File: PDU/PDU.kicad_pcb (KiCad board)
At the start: 2 copper layers, 111 x 127 mm, 82 parts, among them J10 Conn_01x02_Socket, J11 Screw_Terminal_01x02, J12 Conn_01x05_Pin, J2 USB_B_Micro, J3 Screw_Terminal_01x02, J4 Conn_01x03_Socket, J5 Conn_01x02_Socket, J6 Conn_01x02_Socket, J7 Conn_01x02_Socket, J8 Conn_01x02_Socket, J9 Conn_01x02_Socket, Q1 PMOS, Q2 NMOS, Q3 PMOS, U1 TPS564257DRLR, U2 MCP6002-I/P, U5 LM73100RPWR, U6 BQ25172DSGR, U8 MAX20801TPBA+, U9 TPS564257DRLR

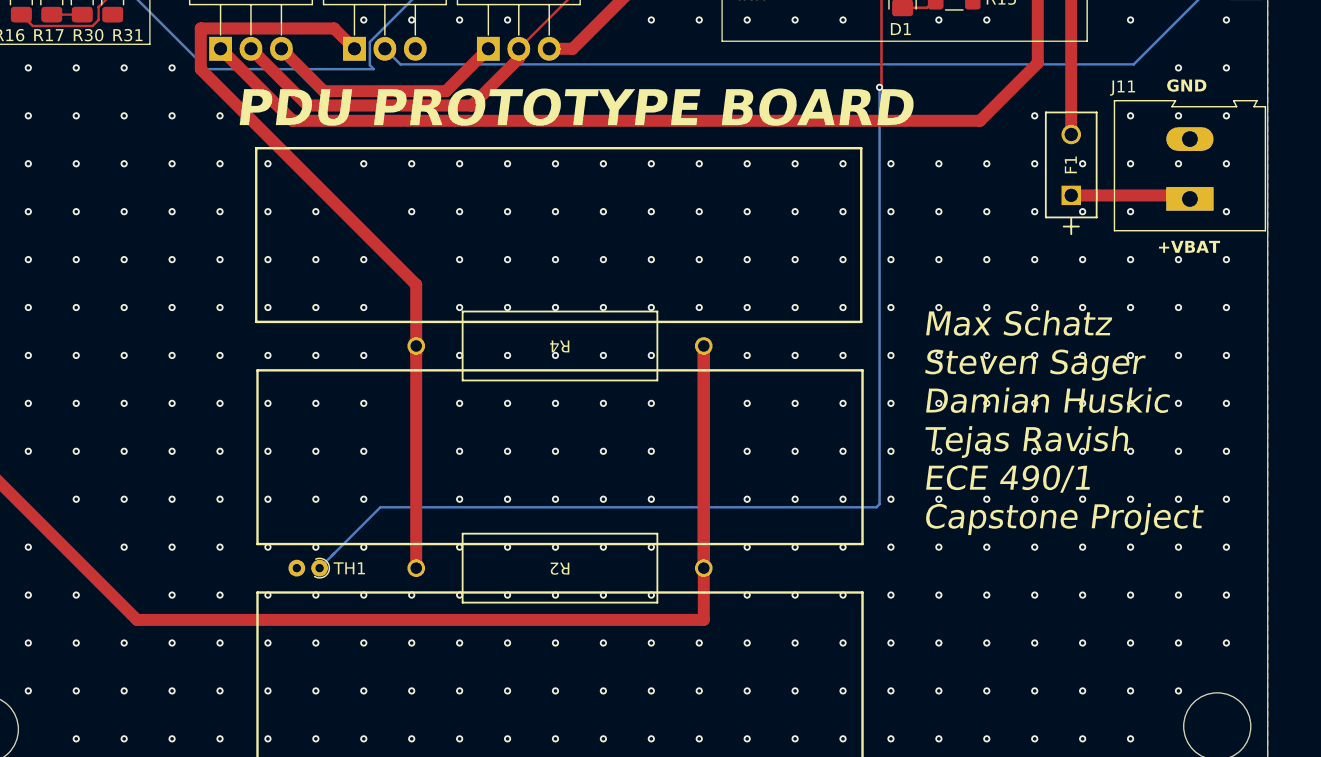
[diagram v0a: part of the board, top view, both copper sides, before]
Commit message: Made revision on PDU board before ECLASS submission
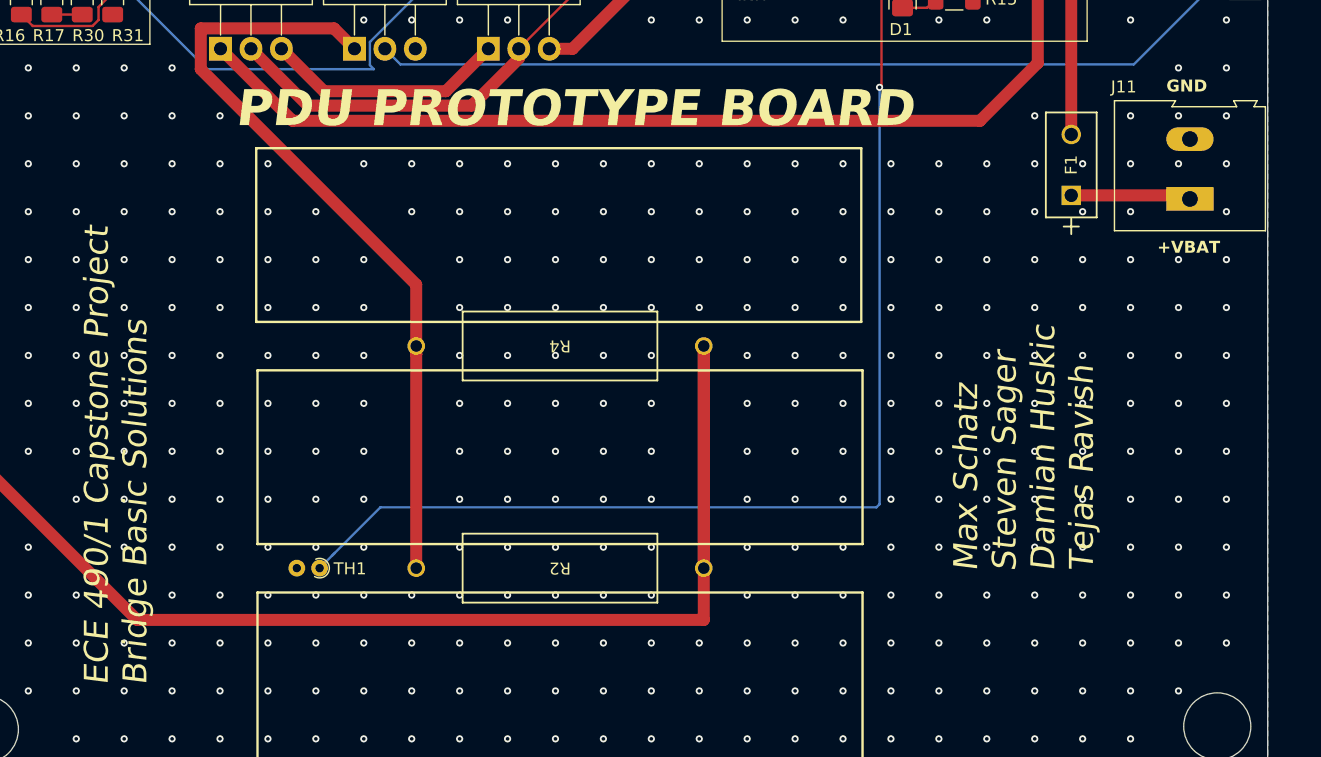
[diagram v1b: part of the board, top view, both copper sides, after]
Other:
- board text added: "ECE 490/1 Capstone Project Bridge Basic Solutions"
- board text added: "Max Schatz Steven Sager Damian Huskic Tejas Ravish"
- board text removed: "Max Schatz Steven Sager Damian Huskic Tejas Ravish ECE 490/1 Capstone Project"
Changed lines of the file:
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@@
+		)
+	)
+	(gr_text "ECE 490/1 Capstone Project\nBridge Basic Solutions"
+		(at 114.5 148.5 90)
+		(layer "F.SilkS")
+		(effects
+			(font
+				(size 2 2)
+				(thickness 0.2)
+				(italic yes)
+			)
+			(justify left bottom)
 		)
 	)
@@
 		)
 	)
-	(gr_text "Max Schatz\nSteven Sager\nDamian Huskic\nTejas Ravish\nECE 490/1\nCapstone Project"
-		(at 179.07 135.636 0)
+	(gr_text "Max Schatz\nSteven Sager\nDamian Huskic\nTejas Ravish"
+		(at 193.5 139 90)
 		(layer "F.SilkS")
 		(effects

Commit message: Last revision
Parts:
- removed C12: 1u, Capacitor_SMD:C_1206_3216Metric_Pad1.33x1.80mm_HandSolder
- removed C13: 0.22u, Capacitor_SMD:C_1206_3216Metric_Pad1.33x1.80mm_HandSolder
- removed C14, C15, C16, C17, C18: 10u, Capacitor_SMD:C_1206_3216Metric_Pad1.33x1.80mm_HandSolder
- removed J10, J7, J8, J9: Conn_01x02_Socket, Connector_PinHeader_2.54mm:PinHeader_1x02_P2.54mm_Vertical
- removed J11: Screw_Terminal_01x02, TerminalBlock:TerminalBlock_Altech_AK300-2_P5.00mm
- removed J12: Conn_01x05_Pin, Connector_PinHeader_2.54mm:PinHeader_1x05_P2.54mm_Vertical
- removed J4: Conn_01x03_Socket, Connector_PinHeader_2.54mm:PinHeader_1x03_P2.54mm_Vertical
- removed L2: 0.68uH, Capstone:IND_RR68M8A_VIS
- removed Q1: PMOS, Package_TO_SOT_THT:TO-220-3_Horizontal_TabDown
- removed Q2: NMOS, Package_TO_SOT_THT:TO-220-3_Horizontal_TabDown
- removed R2, R4: 15, Capstone:res2_1-1625892-1_TEC
- removed TH1: 10k, Resistor_THT:R_Axial_DIN0204_L3.6mm_D1.6mm_P1.90mm_Vertical
- removed U8: MAX20801TPBA+, Capstone:21-100119_MXM
- added C28: 22u, Capacitor_SMD:C_1206_3216Metric_Pad1.33x1.80mm_HandSolder, B.Cu at (145.5, 111.7)
- added C29: 100n, Capacitor_SMD:C_1206_3216Metric_Pad1.33x1.80mm_HandSolder, B.Cu at (145.5, 109.1)
- added C30: 4.7u, Capacitor_SMD:C_1206_3216Metric_Pad1.33x1.80mm_HandSolder, B.Cu at (124.2, 114.1)
- added C31: 100n, Capacitor_SMD:C_1206_3216Metric_Pad1.33x1.80mm_HandSolder, B.Cu at (124.2, 111.6)
- added C32: 100n, Capacitor_SMD:C_1206_3216Metric_Pad1.33x1.80mm_HandSolder, B.Cu at (119.6, 115.4)
- added C33: 22u, Capacitor_SMD:C_1206_3216Metric_Pad1.33x1.80mm_HandSolder, B.Cu at (124.0, 121.2)
- added C34: 22u, Capacitor_SMD:C_1206_3216Metric_Pad1.33x1.80mm_HandSolder, B.Cu at (124.0, 123.8)
- added C6: 10u, Capacitor_SMD:C_1206_3216Metric_Pad1.33x1.80mm_HandSolder, B.Cu at (145.3, 121.8)
- added C7: 100n, Capacitor_SMD:C_1206_3216Metric_Pad1.33x1.80mm_HandSolder, B.Cu at (145.3, 119.3)
- added C8: 10p, Resistor_SMD:R_1206_3216Metric_Pad1.30x1.75mm_HandSolder, B.Cu at (141.7, 110.4)
- added C9: 22u, Capacitor_SMD:C_1206_3216Metric_Pad1.33x1.80mm_HandSolder, B.Cu at (145.5, 114.2)
- added H1: ReedSW MT, Capstone:ReedSW, F.Cu at (161.9, 103.1)
- added H2: ReedSW MT, Capstone:ReedSW, F.Cu at (161.9, 140.9)
- added J1: S5B-PH-K-S, Capstone:CONN_B5B-XH-A_JST, B.Cu at (165.1, 75.3)
- added JP1: SolderJumper_2_Open, Jumper:SolderJumper-2_P1.3mm_Open_TrianglePad1.0x1.5mm, B.Cu at (110.2, 130.8)
- added L4: 4.7u, Inductor_SMD:L_Bourns_SRP7028A_7.3x6.6mm, B.Cu at (137.9, 116.7)
- added L5: 15uH, Capstone:IND_BOURNS_SRR1208, B.Cu at (111.3, 117.4)
- added M1: ~, Capstone:AA_Bat_Contact, F.Cu at (126.7, 98.4)
- added MOSFET1: DMP10H400SK3-13, Capstone:TO252-DPAK-DMP10H400SK3_DIO, B.Cu at (110.2, 81.3)
- added R34: 113k, Resistor_SMD:R_1206_3216Metric_Pad1.30x1.75mm_HandSolder, B.Cu at (150.6, 121.8)
- added R35: 30k, Resistor_SMD:R_1206_3216Metric_Pad1.30x1.75mm_HandSolder, B.Cu at (150.6, 119.3)
- added R36: 10k, Resistor_SMD:R_1206_3216Metric_Pad1.30x1.75mm_HandSolder, B.Cu at (150.6, 116.7)
- added R37: 75.2k, Resistor_SMD:R_1206_3216Metric_Pad1.30x1.75mm_HandSolder, B.Cu at (150.6, 114.2)
- added R38: 10k, Resistor_SMD:R_1206_3216Metric_Pad1.30x1.75mm_HandSolder, B.Cu at (150.6, 111.7)
- added R40: 100k, Resistor_SMD:R_1206_3216Metric_Pad1.30x1.75mm_HandSolder, B.Cu at (132.1, 82.0)
- added R41: 7.15k, Resistor_SMD:R_1206_3216Metric_Pad1.30x1.75mm_HandSolder, B.Cu at (129.3, 121.2)
- added R42: Rent, Resistor_SMD:R_1206_3216Metric_Pad1.30x1.75mm_HandSolder, B.Cu at (129.3, 111.6)
- added R43: Renb, Resistor_SMD:R_1206_3216Metric_Pad1.30x1.75mm_HandSolder, B.Cu at (129.3, 114.1)
- added U3: TPS564257DRLR, Capstone:TPS564242DRLR_TEX, B.Cu at (144.3, 116.8)
- added U4: MCP6001UT-I/OT, Capstone:SOT-23-5_MC_MCH, B.Cu at (143.8, 64.7)
- C1, C10, C11, C2, C20, C22, C23, C24, C27, C3, C4, C5, D1, J2, L1, L3, R10, R11, R12, R13, R14, R15, R16, R17, R19, R20, R22, R23, R24, R25, R26, R27, R28, R29, R30, R31, R32, R33, R5, R6, R7, R8, R9, U1, U5, U6, U9: moved to B.Cu
- C19, C21, C25, C26: footprint Capacitor_SMD:C_0805_2012Metric_Pad1.18x1.45mm_HandSolder -> Capacitor_SMD:C_1206_3216Metric_Pad1.33x1.80mm_HandSolder; moved to B.Cu
- F1: footprint Capstone:FUS_LITTELFUSE_392_LTF -> Fuse:Fuse_2920_7451Metric_Pad2.10x5.45mm_HandSolder; moved to B.Cu
- J3: value Screw_Terminal_01x02 -> 1935310; footprint TerminalBlock:TerminalBlock_Altech_AK300-2_P5.00mm -> Capstone:CONN_1935310_PXC; moved to B.Cu
- J5, J6: value Conn_01x02_Socket -> S2B-PH-K-SLFSN; footprint Connector_PinHeader_2.54mm:PinHeader_1x02_P2.54mm_Vertical -> Capstone:CONN_S2B-PH-K-S_JST
- Q3: value PMOS -> IPD60R2K0PFD7SAUMA1; footprint Package_TO_SOT_THT:TO-220-3_Horizontal_TabDown -> Capstone:DPAK229P994X240-3N; moved to B.Cu
- R1: value 137k -> 113k; moved to B.Cu
- R18: value R -> 100k; footprint Resistor_THT:R_Axial_DIN0309_L9.0mm_D3.2mm_P15.24mm_Horizontal -> Resistor_SMD:R_1206_3216Metric_Pad1.30x1.75mm_HandSolder; moved to B.Cu
- R21: value 220k -> 75.2k; moved to B.Cu
- R3: value 10k -> 10; footprint Resistor_SMD:R_1206_3216Metric_Pad1.30x1.75mm_HandSolder -> Resistor_SMD:R_2512_6332Metric_Pad1.40x3.35mm_HandSolder; moved to B.Cu
- U2: value MCP6002-I/P -> LMR51625XFDDCR; footprint Capstone:PDIP8_300MC_MCH -> Capstone:DDC0006A-MFG; moved to B.Cu
- moved J3 121.9 mm to (117.9, 160.8), turned to 90 degrees
- moved C2 109.2 mm to (145.3, 139.1)
- moved R1 109.2 mm to (150.6, 139.1)
- moved C1 104.5 mm to (145.3, 136.6)
- moved R19 104.5 mm to (150.6, 136.6)
- moved L1 99.8 mm to (137.9, 134.0), turned to 90 degrees
- moved R20 99.8 mm to (150.6, 134.0)
- moved U1 99.6 mm to (144.3, 134.0)
- moved F1 96.1 mm to (114.3, 50.4)
- moved R21 95.2 mm to (150.6, 131.5)
- moved C21 94.5 mm to (145.5, 131.5), turned to 0 degrees
- moved C10 92.5 mm to (120.4, 144.3), turned to -90 degrees
- moved R29 92.5 mm to (117.9, 144.3), turned to 90 degrees
- moved R8 92.5 mm to (115.4, 144.3), turned to -90 degrees
- moved R22 90.6 mm to (150.6, 128.9)
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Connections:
- C1 pad 1: Net-(J9-Pin_2) -> /Converters/VIN
- C2 pad 1: Net-(J9-Pin_2) -> /Converters/VIN
- C22 pad 1: Net-(J8-Pin_2) -> /Converters/VIN
- C23 pad 1: Net-(J8-Pin_2) -> /Converters/VIN
- C4 pad 1: /NiMH Charger/IN -> /Ideal Diode/IN
- F1 pad 2: /NiMH Charger/OUT -> /VBAT_Monitor/VBAT_IN
- J2 pad 1: /MPPT/MPPT_OUT -> /MPPT/+12V
- J3 pad 1: Net-(J3-Pin_1) -> /MPPT/VIN
- J5 pad 1: Net-(J5-Pin_1) -> +5V_HEATER
- J5 pad 2: /MPPT/MPPT_OUT -> Net-(J5-Pad2)
- J6 pad 1: /MPPT/MPPT_OUT -> GND
- J6 pad 2: /NiMH Charger/IN -> Net-(U6-TS)
- Q3 pad 1: Net-(Q1-S) -> /PWM_HEATER
- Q3 pad 3: /Converters/VIN -> GND
- R1 pad 1: Net-(J9-Pin_2) -> /Converters/VIN
- R16 pad 1: /NiMH Charger/OUT -> /VBAT_Monitor/VBAT_IN
- R18 pad 1: Net-(J3-Pin_1) -> /MPPT/+12V
- R18 pad 2: Net-(J4-Pin_2) -> Net-(U2-FB)
- R23 pad 1: Net-(J8-Pin_2) -> /Converters/VIN
- R3 pad 1: /Ideal Diode/IN -> /NiMH Charger/OUT
- R3 pad 2: Net-(Q1-G) -> /VBAT_Monitor/VBAT_IN
- U1 pad 1: Net-(J9-Pin_2) -> /Converters/VIN
- U2 pad 1: /VBAT_SENSE -> Net-(U2-FB)
- U2 pad 2: /VBAT_SENSE -> Net-(U2-EN)
- U2 pad 3: /VBAT_Monitor/VINA+ -> /MPPT/VIN
- U2 pad 5: +5V -> Net-(U2-SW)
- U2 pad 6: GND -> Net-(U2-CB)
- U6 pad 1: /NiMH Charger/IN -> /Ideal Diode/IN
- U9 pad 1: Net-(J8-Pin_2) -> /Converters/VIN
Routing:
- net +5V: track 301.0 -> 127.3 mm, vias 0 -> 1
- net /MPPT/+12V: track 0.00 -> 153.6 mm, vias 0 -> 2
- net /MPPT/MPPT_OUT: track 142.0 -> 0.00 mm
- net +5V_HEATER: track 0.00 -> 130.8 mm, vias 0 -> 1
- net Net-(J5-Pad2): track 0.00 -> 101.3 mm
- net /MPPT/VIN: track 0.00 -> 92.2 mm
- net Net-(J7-Pin_2): track 83.1 -> 0.00 mm
- net /VBAT_SENSE: track 118.3 -> 37.6 mm, vias 0 -> 1
- net /Ideal Diode/IN: track 46.3 -> 115.8 mm
- net Net-(Q2-D): track 66.0 -> 0.00 mm
- net /VBAT_Monitor/VBAT_IN: track 0.00 -> 54.2 mm
- net +3.3V: track 79.8 -> 131.7 mm
- net Net-(Q1-G): track 38.2 -> 0.00 mm
- net /Converters/VIN: track 87.3 -> 123.0 mm, vias 2 -> 0
- net Net-(U6-TS): track 97.0 -> 61.6 mm
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- added copper zone on B.Cu, net +3.3V
- added copper zone on B.Cu, net +5V
- added copper zone on B.Cu, net +5V_HEATER
- added copper zone on B.Cu, net /Converters/VIN
- added copper zone on B.Cu, net /Ideal Diode/IN
- added copper zone on B.Cu, net /MPPT/+12V
- added copper zone on B.Cu, net /MPPT/VIN
- added copper zone on B.Cu, net /NiMH Charger/OUT
- added copper zone on B.Cu, net Net-(U1-SW)
- added copper zone on B.Cu, net Net-(U2-SW)
- added copper zone on B.Cu, net Net-(U3-SW)
- added copper zone on B.Cu, net Net-(U9-SW)
- removed copper zone on F.Cu, net +3.3V
- removed copper zone on F.Cu, net +5V
- removed copper zone on F.Cu, net /Converters/VIN
- removed copper zone on F.Cu, net /Ideal Diode/IN
- removed copper zone on F.Cu, net /MPPT/PV+
- removed copper zone on F.Cu, net /NiMH Charger/IN
- removed copper zone on F.Cu, net /NiMH Charger/OUT
- removed copper zone on F.Cu, net Net-(J3-Pin_1)
- removed copper zone on F.Cu, net Net-(J4-Pin_2)
- removed copper zone on F.Cu, net Net-(J5-Pin_1)
- removed copper zone on F.Cu, net Net-(J8-Pin_2)
- removed copper zone on F.Cu, net Net-(J9-Pin_2)
- removed copper zone on F.Cu, net Net-(U1-SW)
- removed copper zone on F.Cu, net Net-(U8-OUT)
- removed copper zone on F.Cu, net Net-(U9-SW)
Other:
- board size 111 x 127 mm -> 70 x 130 mm
- board text added: "CHARGE"
- board text added: "ECE 490/1 CAPSTONE SSULPEP PDU BRIDGE BASIC SOLUTIONS"
- board text added: "HEATER"
- board text added: "PDU BOARD"
- board text added: "PV+"
- board text added: "PV-"
- board text added: "THERM"
- board text removed: "+PV"
- board text removed: "+VBAT"
- board text removed: "-PV (GND)"
- board text removed: "3V3 CONVERTER"
- board text removed: "5V CONVERTER"
- board text removed: "BATTERY CHARGER"
- board text removed: "BYPASS"
- board text removed: "ECE 490/1 Capstone Project Bridge Basic Solutions"
- board text removed: "INH"
- board text removed: "INHIBIT CIRCUIT"
- board text removed: "MPPT CONVERTER"
- board text removed: "MPPT INH"
- board text removed: "PDU PROTOTYPE BOARD"
- board text removed: "VBAT MONITOR"
